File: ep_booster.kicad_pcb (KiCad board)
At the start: 2 copper layers, 45 x 21.2 mm, 31 parts, among them J1 TB002-500-04BE, J2 Conn_01x04_Pin, Q1 MMBF5457, Q2 BC849C

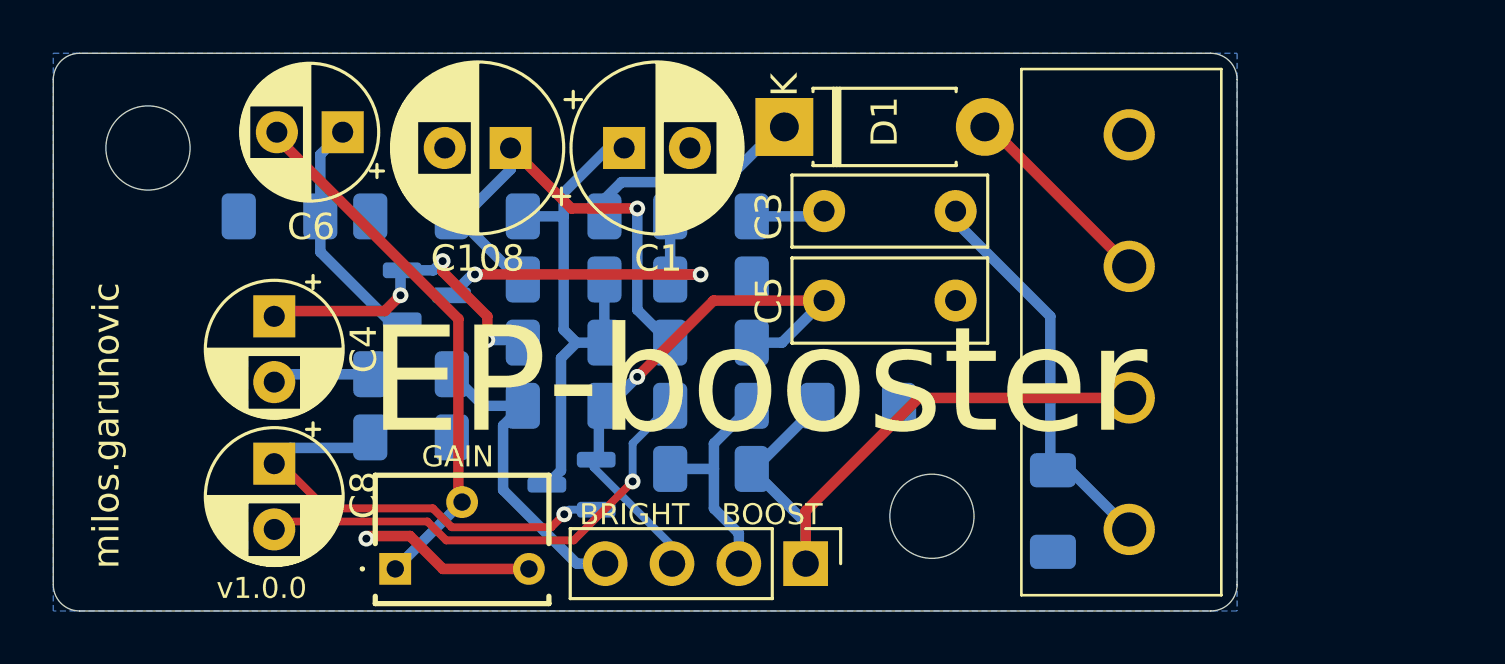
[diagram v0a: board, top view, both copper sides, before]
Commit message: increase track width to 0.4mm
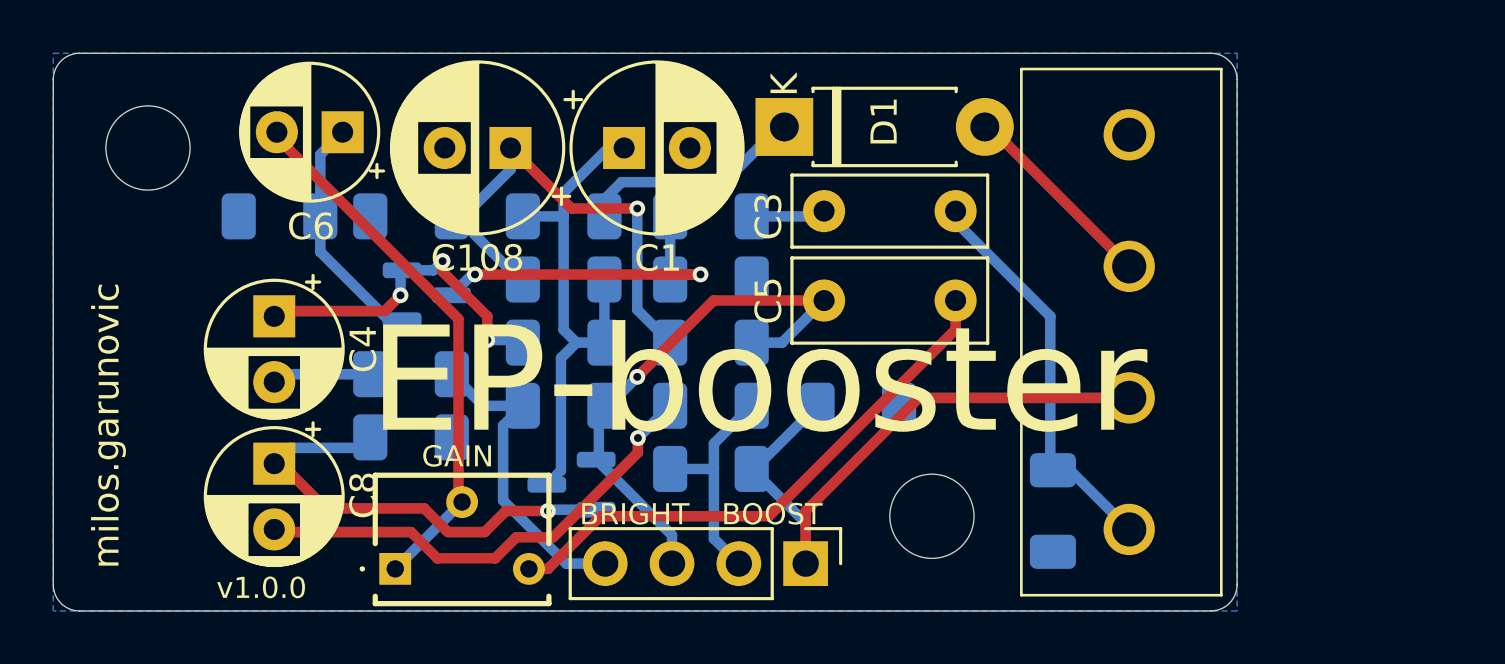
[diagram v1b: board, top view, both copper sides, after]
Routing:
- net GND: track 6.74 -> 21.1 mm, vias 1 -> 0
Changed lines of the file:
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@@
 			(pinfunction "3")
 			(pintype "passive")
-			(zone_connect 2)
+			(zone_connect 0)
 		)
 		(model "3362S-1-103LF.stp"
@@
 			(net 1 "GND")
 			(pintype "passive")
+			(zone_connect 2)
 		)
 		(model "${KICAD8_3DMODEL_DIR}/Resistor_SMD.3dshapes/R_1206_3216Metric.wrl"
@@
 	)
 	(segment
-		(start 186.6 93.55)
-		(end 188.16 93.55)
+		(start 201.8 92.8)
+		(end 208.9 85.7)
 		(width 0.4)
 		(layer "F.Cu")
@@
 	)
 	(segment
-		(start 189.41 94.8)
-		(end 192.68 94.8)
+		(start 193.4 94.8)
+		(end 195.4 92.8)
 		(width 0.4)
 		(layer "F.Cu")
@@
 	)
 	(segment
-		(start 188.16 93.55)
-		(end 189.41 94.8)
+		(start 192.68 94.8)
+		(end 193.4 94.8)
 		(width 0.4)
 		(layer "F.Cu")
@@
 	)
 	(segment
-		(start 186.5 93.65)
-		(end 186.6 93.55)
+		(start 208.9 85.7)
+		(end 208.9 84.6)
 		(width 0.4)
 		(layer "F.Cu")
 		(net 1)
 	)
-	(via
-		(at 186.5 93.65)
-		(size 0.6)
-		(drill 0.3)
-		(layers "F.Cu" "B.Cu")
+	(segment
+		(start 195.4 92.8)
+		(end 201.8 92.8)
+		(width 0.4)
+		(layer "F.Cu")
 		(net 1)
 	)
@@
 	)
 	(segment
-		(start 189.744426 93.215)
-		(end 193.5333 93.215)
-		(width 0.3)
+		(start 184.95085 92.5)
+		(end 183.25085 90.8)
+		(width 0.4)
+		(layer "F.Cu")
+		(net 8)
+	)
+	(segment
+		(start 189.6 93.4)
+		(end 188.7 92.5)
+		(width 0.4)
 		(layer "F.Cu")
 		(net 8)
@@
 	(segment
 		(start 183.25085 90.8)
-		(end 184.95085 92.5)
-		(width 0.3)
+		(end 183 90.8)
+		(width 0.4)
 		(layer "F.Cu")
 		(net 8)
 	)
 	(segment
-		(start 184.95085 92.5)
-		(end 189.029426 92.5)
-		(width 0.3)
+		(start 191.8 92.6)
+		(end 191 93.4)
+		(width 0.4)
 		(layer "F.Cu")
 		(net 8)
 	)
 	(segment
-		(start 183 90.8)
-		(end 183.25085 90.8)
-		(width 0.3)
+		(start 191 93.4)
+		(end 189.6 93.4)
+		(width 0.4)
 		(layer "F.Cu")
 		(net 8)
 	)
 	(segment
-		(start 193.5333 93.215)
-		(end 194.0237 92.7246)
-		(width 0.3)
+		(start 193.4 92.6)
+		(end 191.8 92.6)
+		(width 0.4)
 		(layer "F.Cu")
 		(net 8)
 	)
 	(segment
-		(start 189.029426 92.5)
-		(end 189.744426 93.215)
-		(width 0.3)
+		(start 188.7 92.5)
+		(end 184.95085 92.5)
+		(width 0.4)
 		(layer "F.Cu")
 		(net 8)
 	)
 	(via
-		(at 194.0237 92.7246)
+		(at 193.4 92.6)
 		(size 0.6)
 		(drill 0.3)
@@
 	)
 	(segment
-		(start 194.1983 92.55)
-		(end 194.0237 92.7246)
-		(width 0.3)
-		(layer "B.Cu")
-		(net 8)
-	)
-	(segment
-		(start 195.2375 92.55)
-		(end 194.1983 92.55)
-		(width 0.3)
+		(start 186.1017 90.2)
+		(end 186.5017 89.8)
+		(width 0.4)
 		(layer "B.Cu")
 		(net 8)
 	)
 	(segment
-		(start 186.1017 90.2)
-		(end 186.5017 89.8)
+		(start 193.45 92.55)
+		(end 195.2375 92.55)
 		(width 0.4)
 		(layer "B.Cu")
@@
 	)
 	(segment
+		(start 193.4 92.6)
+		(end 193.45 92.55)
+		(width 0.4)
+		(layer "B.Cu")
+		(net 8)
+	)
+	(segment
 		(start 196.8 81.0995)
 		(end 194.2995 81.0995)
@@
 	)
 	(segment
-		(start 199.7125 91)
-		(end 199.7125 92.5008)
-		(width 0.4)
-		(layer "B.Cu")
-		(net 14)
-	)
-	(segment
 		(start 201.15 88.6)
 		(end 199.7125 90.0375)
@@
 	)
 	(segment
-		(start 199.7125 90.0375)
-		(end 199.7125 91)
+		(start 199.7125 93.6525)
+		(end 200.66 94.6)
 		(width 0.4)
 		(layer "B.Cu")
@@
 	)
 	(segment
-		(start 200.66 94.6)
-		(end 200.66 93.4483)
+		(start 199.7125 90.0375)
+		(end 199.7125 91)
 		(width 0.4)
 		(layer "B.Cu")
@@
 	)
 	(segment
-		(start 199.7125 92.5008)
-		(end 200.66 93.4483)
+		(start 199.7125 91)
+		(end 199.7125 93.6525)
 		(width 0.4)
 		(layer "B.Cu")
@@
 	)
 	(segment
-		(start 195.1375 90.9396)
-		(end 195.1375 90.8417)
-		(width 0.3)
-		(layer "B.Cu")
-		(net 15)
-	)
-	(segment
 		(start 195.3375 88.8125)
 		(end 195.3375 90.55)
@@
 	)
 	(segment
+		(start 195.25 90.65)
+		(end 198.12 93.52)
+		(width 0.4)
+		(layer "B.Cu")
+		(net 15)
+	)
+	(segment
 		(start 195.7 88.6)
 		(end 195.55 88.6)
@@
 	)
 	(segment
-		(start 198.12 93.9221)
-		(end 195.1375 90.9396)
-		(width 0.3)
+		(start 195.55 88.6)
+		(end 195.3375 88.8125)
+		(width 0.2)
 		(layer "B.Cu")
 		(net 15)
 	)
 	(segment
-		(start 195.55 88.6)
-		(end 195.3375 88.8125)
-		(width 0.2)
+		(start 195.2375 90.65)
+		(end 195.25 90.65)
+		(width 0.4)
 		(layer "B.Cu")
 		(net 15)
@@
 	)
 	(segment
+		(start 198.12 93.52)
+		(end 198.12 93.9221)
+		(width 0.4)
+		(layer "B.Cu")
+		(net 15)
+	)
+	(segment
 		(start 195.1375 90.75)
 		(end 195.2375 90.65)
@@
 	)
 	(segment
-		(start 191.7 91.8)
-		(end 194.5 94.6)
+		(start 194.1 94.6)
+		(end 195.58 94.6)
 		(width 0.4)
 		(layer "B.Cu")
@@
 	)
 	(segment
-		(start 194.5 94.6)
-		(end 195.58 94.6)
+		(start 191.7 92.2)
+		(end 194.1 94.6)
 		(width 0.4)
 		(layer "B.Cu")
@@
 	(segment
 		(start 191.7 89.35)
-		(end 191.7 91.8)
+		(end 191.7 92.2)
 		(width 0.4)
 		(layer "B.Cu")
@@
 	)
 	(segment
-		(start 194.385 93.715)
-		(end 189.53732 93.715)
-		(width 0.3)
+		(start 196.825 89.825)
+		(end 196.825 90.375)
+		(width 0.4)
 		(layer "F.Cu")
 		(net 18)
 	)
 	(segment
-		(start 183.3 93)
-		(end 183 93.3)
-		(width 0.3)
+		(start 188.2 93.4)
+		(end 183.1 93.4)
+		(width 0.4)
 		(layer "F.Cu")
 		(net 18)
 	)
 	(segment
-		(start 188.82232 93)
-		(end 183.3 93)
-		(width 0.3)
+		(start 196.825 90.375)
+		(end 193.6 93.6)
+		(width 0.4)
 		(layer "F.Cu")
 		(net 18)
 	)
 	(segment
-		(start 196.6233 91.4767)
-		(end 194.385 93.715)
-		(width 0.3)
+		(start 191.4 94.4)
+		(end 189.2 94.4)
+		(width 0.4)
 		(layer "F.Cu")
 		(net 18)
 	)
 	(segment
-		(start 189.53732 93.715)
-		(end 188.82232 93)
-		(width 0.3)
+		(start 193.6 93.6)
+		(end 192.2 93.6)
+		(width 0.4)
+		(layer "F.Cu")
+		(net 18)
+	)
+	(segment
+		(start 189.2 94.4)
+		(end 188.2 93.4)
+		(width 0.4)
+		(layer "F.Cu")
+		(net 18)
+	)
+	(segment
+		(start 183.1 93.4)
+		(end 183 93.3)
+		(width 0.4)
+		(layer "F.Cu")
+		(net 18)
+	)
+	(segment
+		(start 192.2 93.6)
+		(end 191.4 94.4)
+		(width 0.4)
 		(layer "F.Cu")
 		(net 18)
 	)
 	(via
-		(at 196.6233 91.4767)
+		(at 196.825 89.825)
 		(size 0.6)
 		(drill 0.3)
@@
 	)
 	(segment
-		(start 198.05 88.6)
-		(end 196.6233 90.0267)
-		(width 0.3)
-		(layer "B.Cu")
-		(net 18)
-	)
-	(segment
-		(start 196.6233 90.0267)
-		(end 196.6233 91.4767)
-		(width 0.3)
+		(start 196.825 89.825)
+		(end 198.05 88.6)
+		(width 0.4)
 		(layer "B.Cu")
 		(net 18)

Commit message: add F.Silkscreen for IO, update C ref des
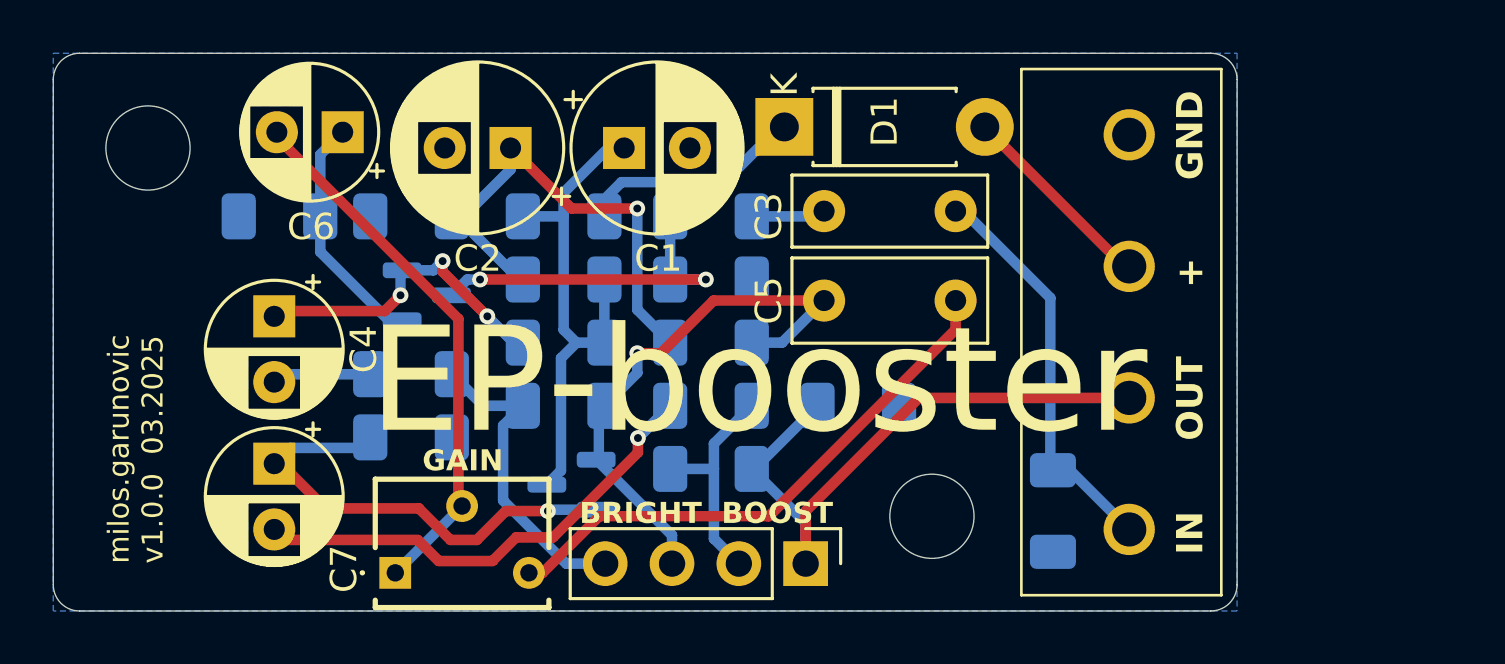
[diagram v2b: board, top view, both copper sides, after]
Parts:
- moved RV1 0.15 mm to (187.6, 95.0)
- renumbered C108 to C2, C8 to C7
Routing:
- net Net-(Q1-D): track 12.9 -> 12.4 mm
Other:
- board text added: "milos.garunovic v1.0.0 03.2025"
- board text removed: "milos.garunovic"
- board text removed: "v1.0.0"
